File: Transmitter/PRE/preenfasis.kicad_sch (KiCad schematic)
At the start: 24 parts, among them J1 SMA H, J2 SMA H, J3 SMA H, J4 SMA H

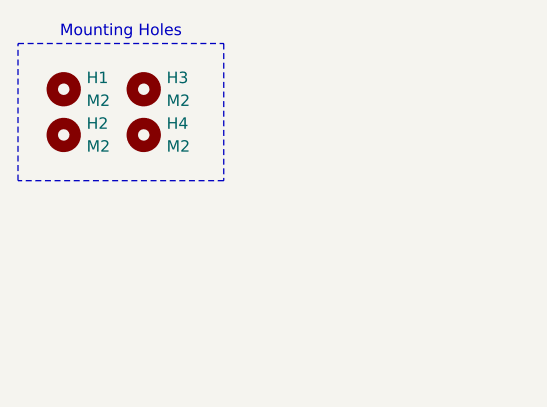
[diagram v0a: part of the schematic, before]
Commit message: v1.2 preenfasis
Se cambia el tamaño de los tornillos de M2 a M3
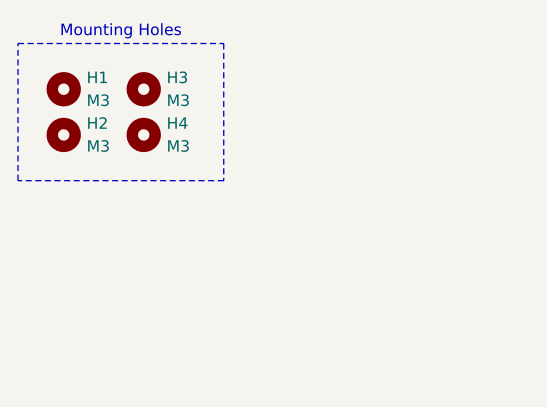
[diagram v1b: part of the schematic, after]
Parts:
- H1, H2, H3, H4: value M2 -> M3; footprint MountingHole:MountingHole_2.2mm_M2_ISO7380 -> MountingHole:MountingHole_3.2mm_M3_ISO7380
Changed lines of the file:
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@@
 	(title_block
 		(title "Filtro de preenfasis")
-		(date "2025-01-06")
-		(rev "v1.1")
+		(date "2025-01-09")
+		(rev "v1.2")
 		(company "Cotti Nicolas Gabriel")
 		(comment 1 "ncotti@frba.utn.edu.ar")
@@
 			)
 		)
-		(property "Value" "M2"
+		(property "Value" "M3"
 			(at 31.75 27.9399 0)
 			(effects
@@
 			)
 		)
-		(property "Footprint" "MountingHole:MountingHole_2.2mm_M2_ISO7380"
+		(property "Footprint" "MountingHole:MountingHole_3.2mm_M3_ISO7380"
 			(at 29.21 26.67 0)
 			(effects
@@
 			)
 		)
-		(property "Value" "M2"
+		(property "Value" "M3"
 			(at 22.86 22.8599 0)
 			(effects
@@
 			)
 		)
-		(property "Footprint" "MountingHole:MountingHole_2.2mm_M2_ISO7380"
+		(property "Footprint" "MountingHole:MountingHole_3.2mm_M3_ISO7380"
 			(at 20.32 21.59 0)
 			(effects
@@
 			)
 		)
-		(property "Value" "M2"
+		(property "Value" "M3"
 			(at 31.75 22.8599 0)
 			(effects
@@
 			)
 		)
-		(property "Footprint" "MountingHole:MountingHole_2.2mm_M2_ISO7380"
+		(property "Footprint" "MountingHole:MountingHole_3.2mm_M3_ISO7380"
 			(at 29.21 21.59 0)
 			(effects
@@
 			)
 		)
-		(property "Value" "M2"
+		(property "Value" "M3"
 			(at 22.86 27.9399 0)
 			(effects
@@
 			)
 		)
-		(property "Footprint" "MountingHole:MountingHole_2.2mm_M2_ISO7380"
+		(property "Footprint" "MountingHole:MountingHole_3.2mm_M3_ISO7380"
 			(at 20.32 26.67 0)
 			(effects
